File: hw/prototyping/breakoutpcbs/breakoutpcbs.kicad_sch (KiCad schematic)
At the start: 0 parts

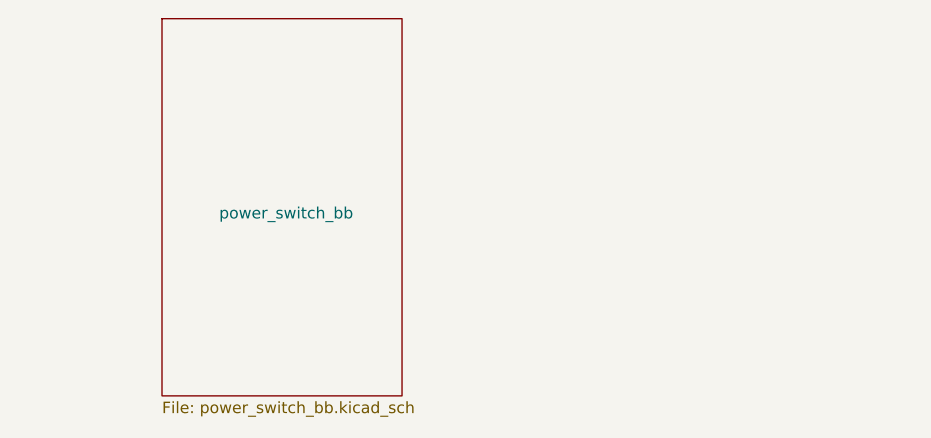
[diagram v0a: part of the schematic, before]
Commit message: created two other modules to test the switching between charging and runnig mode
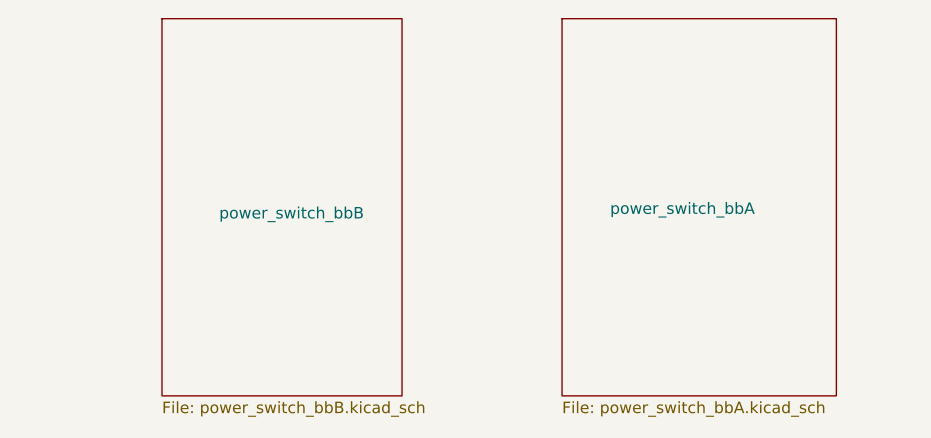
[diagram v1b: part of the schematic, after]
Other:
- sheet power_switch_bb renamed power_switch_bbB
- added sheet power_switch_bbA (power_switch_bbA.kicad_sch)
- sheet power_switch_bbB: file power_switch_bb.kicad_sch -> power_switch_bbB.kicad_sch
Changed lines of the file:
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@@
 	(paper "A4")
+	(sheet
+		(at 138.43 71.12)
+		(size 30.48 41.91)
+		(exclude_from_sim no)
+		(in_bom yes)
+		(on_board yes)
+		(dnp no)
+		(stroke
+			(width 0.1524)
+			(type solid)
+		)
+		(fill
+			(color 0 0 0 0.0000)
+		)
+		(property "Sheetname" "power_switch_bbA"
+			(at 143.764 92.964 0)
+			(effects
+				(font
+					(size 1.27 1.27)
+				)
+				(justify left bottom)
+			)
+		)
+		(property "Sheetfile" "power_switch_bbA.kicad_sch"
+			(at 138.43 113.6146 0)
+			(effects
+				(font
+					(size 1.27 1.27)
+				)
+				(justify left top)
+			)
+		)
+		(instances
+			(project "breakoutpcbs"
+				(path "/164def8b-47e5-45df-ad5a-f5307e8b0f23"
+					(page "4")
+				)
+			)
+		)
+	)
 	(sheet
 		(at 93.98 71.12)
@@
 			(color 0 0 0 0.0000)
 		)
-		(property "Sheetname" "power_switch_bb"
+		(property "Sheetname" "power_switch_bbB"
 			(at 100.33 93.472 0)
 			(effects
@@
 			)
 		)
-		(property "Sheetfile" "power_switch_bb.kicad_sch"
+		(property "Sheetfile" "power_switch_bbB.kicad_sch"
 			(at 93.98 113.6146 0)
 			(effects

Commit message: refactoring of the current boards and two added to test the whole circuit
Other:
- added sheet battery_charger (battery_charger.kicad_sch)
- added sheet break_control (break_control.kicad_sch)
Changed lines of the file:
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@@
+	)
+	(sheet
+		(at 229.87 68.58)
+		(size 34.29 48.26)
+		(exclude_from_sim no)
+		(in_bom yes)
+		(on_board yes)
+		(dnp no)
+		(stroke
+			(width 0.1524)
+			(type solid)
+		)
+		(fill
+			(color 0 0 0 0.0000)
+		)
+		(property "Sheetname" "break_control"
+			(at 241.554 94.742 0)
+			(effects
+				(font
+					(size 1.27 1.27)
+				)
+				(justify left bottom)
+			)
+		)
+		(property "Sheetfile" "break_control.kicad_sch"
+			(at 229.87 117.4246 0)
+			(effects
+				(font
+					(size 1.27 1.27)
+				)
+				(justify left top)
+			)
+		)
+		(instances
+			(project "breakoutpcbs"
+				(path "/164def8b-47e5-45df-ad5a-f5307e8b0f23"
+					(page "6")
+				)
+			)
+		)
 	)
 	(sheet
@@
 				)
 			)
+		)
+	)
+	(sheet
+		(at 181.61 69.85)
+		(size 27.94 46.99)
+		(exclude_from_sim no)
+		(in_bom yes)
+		(on_board yes)
+		(dnp no)
+		(stroke
+			(width 0.1524)
+			(type solid)
+		)
+		(fill
+			(color 0 0 0 0.0000)
+		)
+		(property "Sheetname" "battery_charger"
+			(at 188.722 94.742 0)
+			(effects
+				(font
+					(size 1.27 1.27)
+				)
+				(justify left bottom)
+			)
+		)
+		(property "Sheetfile" "battery_charger.kicad_sch"
+			(at 181.61 117.4246 0)
+			(effects
+				(font
+					(size 1.27 1.27)
+				)
+				(justify left top)
+			)
+		)
+		(instances
+			(project "breakoutpcbs"
+				(path "/164def8b-47e5-45df-ad5a-f5307e8b0f23"
+					(page "5")
+				)
+			)
